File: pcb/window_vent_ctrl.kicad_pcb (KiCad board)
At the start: 2 copper layers, 70 x 50 mm, 32 parts, among them J1 12V IN, J2 FAN 0 intake, J3 FAN 1 exhaust, J4 MOTOR, J5 SCD40, J6 AS5600, J7 DS18B20 in, J8 DS18B20 out, U1 Freenove ESP32-S3 Lite, U2 TMC2209 module

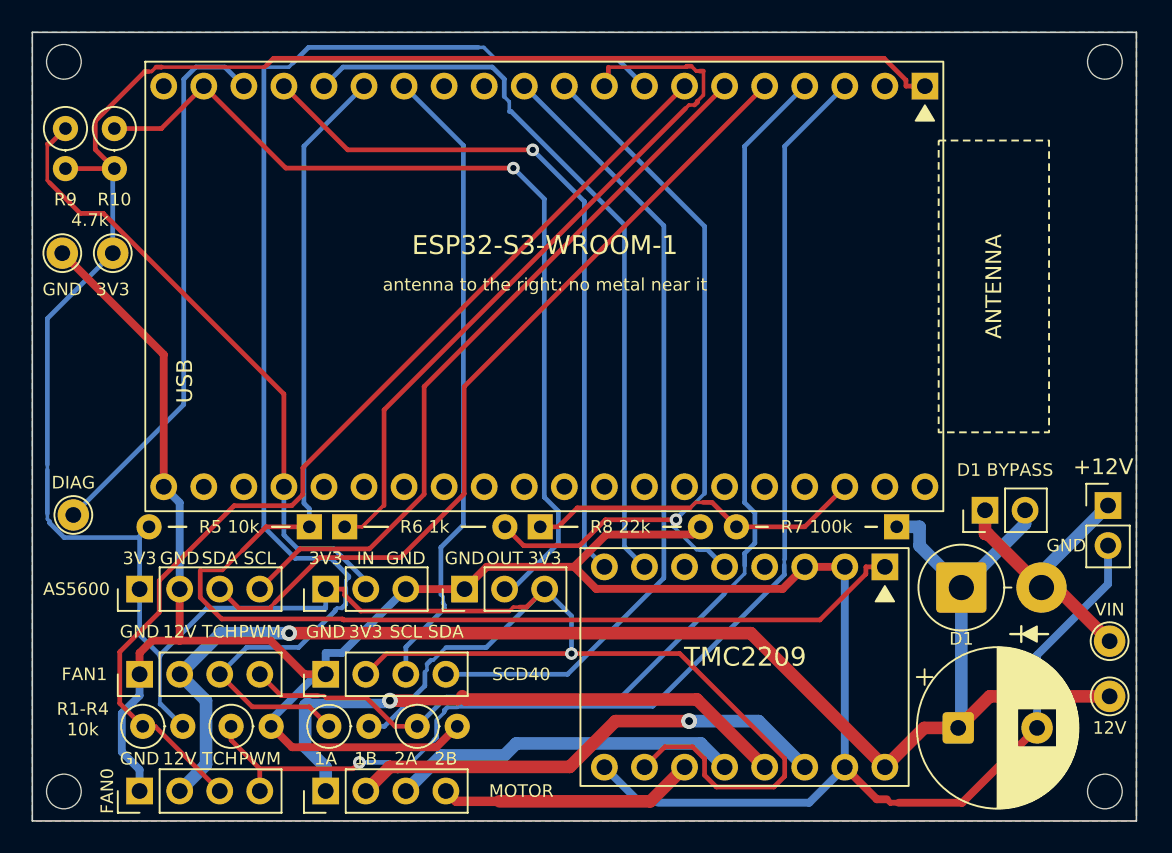
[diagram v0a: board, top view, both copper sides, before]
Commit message: PCB silkscreen: USB-UART cue, TEMP bracket, orientation sketch
Front: "USB-UART" at the board edge beside the ESP32's USB-UART connector
(replacing the footprint's "USB"); a dotted bracket from J7 and J8 to
"TEMP"; SCD40 and MOTOR at FAN1's spacing; FAN1/SCD40 pin labels at the
same 2 mm as the other rows; C1's "+", J1's GND and D1 moved clear.
Back: title and URL clear of the vias, with a small sketch of the board
between "outdoor (top edge)" and "indoor (bottom edge)". DRC clean.

Co-Authored-By: Claude Opus 5.5 <noreply@anthropic.com>
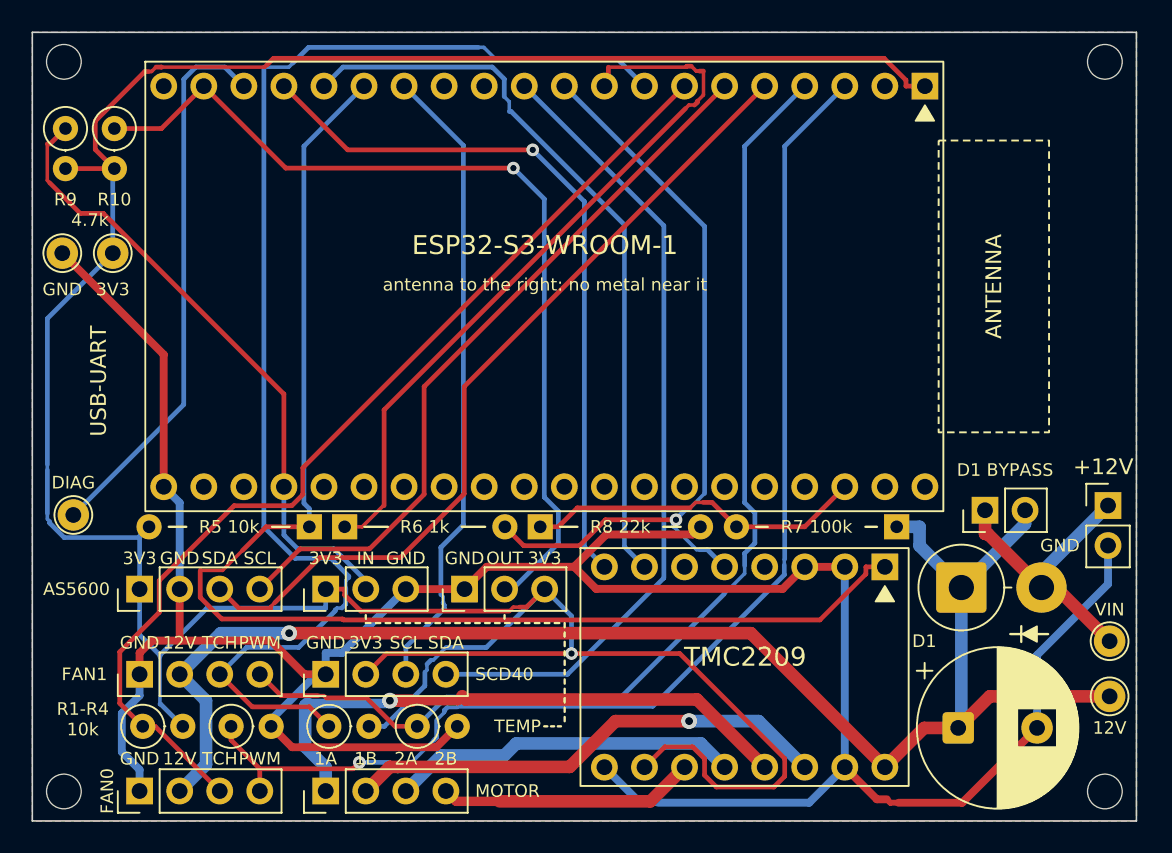
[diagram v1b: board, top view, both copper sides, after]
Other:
- board text added: "TEMP"
- board text added: "USB-UART"
- board text added: "indoor (bottom edge)"
- board text added: "outdoor (top edge)"
- board text added: "this PCB"
- board text removed: "J7: DS18B20 in (GPIO 21) J8: DS18B20 out (GPIO 14) C1: 220 uF 50 V"
- board text removed: "room side (bottom edge)"
- board text removed: "window side (top edge)"

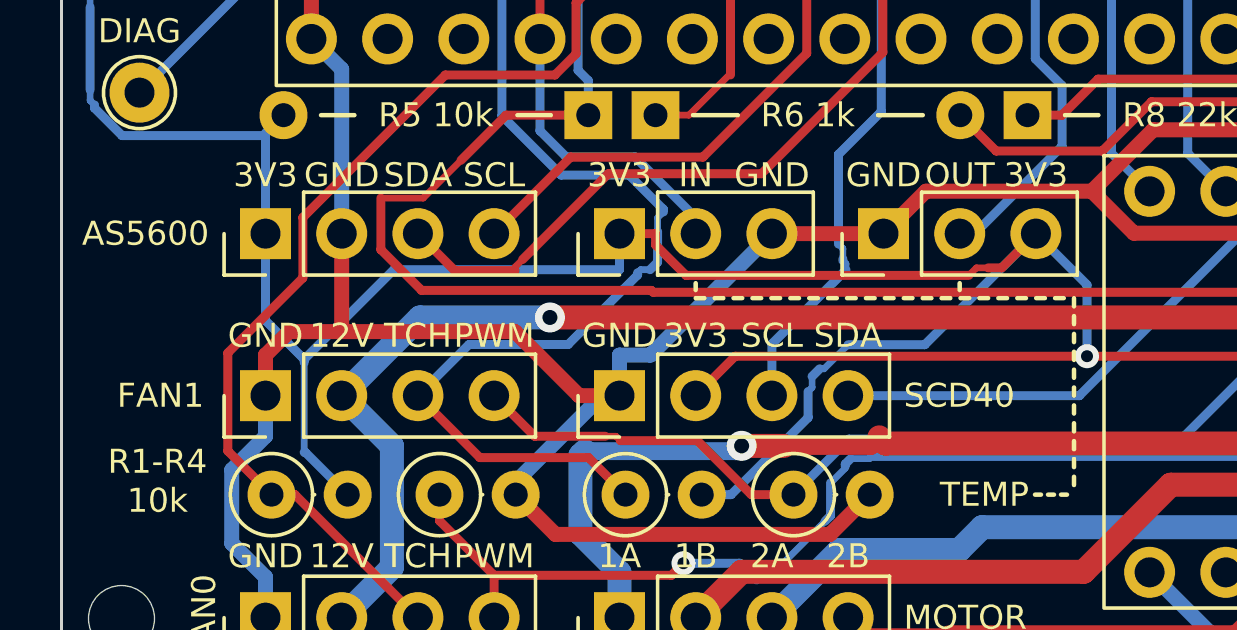
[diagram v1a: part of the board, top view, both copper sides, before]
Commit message: PCB silkscreen: FAN1 down arrow, AS5600 POS and SCD40 CO2 labels
A small down triangle above FAN1 (the exhaust, the bottom duct); a second
line under AS5600 ("POS") and SCD40 ("CO2", with a subscript 2). DRC clean.

Co-Authored-By: Claude Opus 5.5 <noreply@anthropic.com>
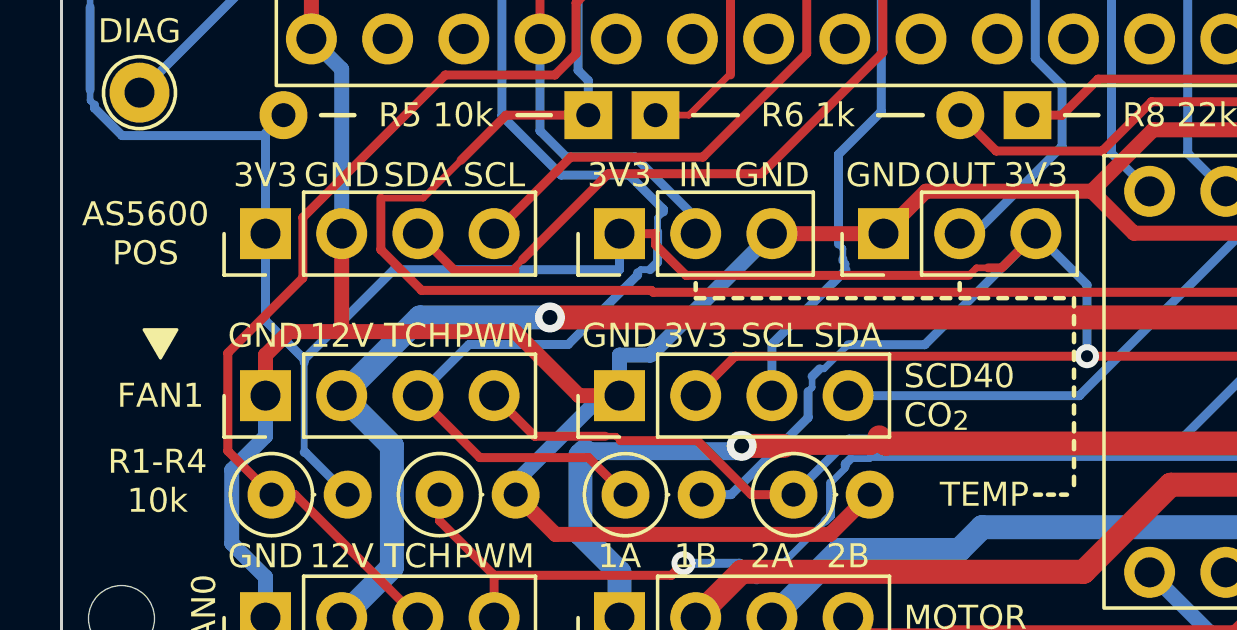
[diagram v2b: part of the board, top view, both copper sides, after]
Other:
- board text added: "CO_{2}"
- board text added: "POS"
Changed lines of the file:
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@@
+	(gr_poly
+		(pts
+			(xy 102.75 138.5) (xy 103.85 138.5) (xy 103.3 139.45)
+		)
+		(stroke
+			(width 0.1)
+			(type default)
+		)
+		(fill yes)
+		(layer "F.SilkS")
+	)
 	(gr_poly
 		(pts
@@
 		(layer "Edge.Cuts")
 	)
+	(gr_text "CO_{2}"
+		(at 128.074286 141.35 0)
+		(layer "F.SilkS")
+		(effects
+			(font
+				(size 0.8 0.8)
+				(thickness 0.15)
+			)
+			(justify left)
+		)
+	)
 	(gr_text "GND"
 		(at 101.9 116.3 0)
@@
 		)
 	)
+	(gr_text "POS"
+		(at 102.8 135.95 0)
+		(layer "F.SilkS")
+		(effects
+			(font
+				(size 0.8 0.8)
+				(thickness 0.15)
+			)
+		)
+	)
 	(gr_text "R1-R4"
 		(at 103.2 142.9 0)
@@
 	)
 	(gr_text "SCD40"
-		(at 128.074286 140.7 0)
+		(at 128.074286 140.05 0)
 		(layer "F.SilkS")
 		(effects
@@
 	)
 	(gr_text "AS5600"
-		(at 102.8 135.3 0)
-		(layer "F.SilkS")
-		(effects
+		(at 102.8 134.65 0)
+		(layer "F.SilkS")
+		(effects

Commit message: Controller PCB v1.1: solder jumper JP2 joins GPIO 21 to GPIO 3 (audio mode)
JP2, open by default, on the back under the ESP32: bridge it to read a
microphone on J7 with GPIO 3 (ADC1). The board is re-routed; the routing
now keeps vias off every silkscreen label. The v1.0 Gerber zip stays (the
boards already ordered). Docs, Pins.h and the wiring diagram mention JP2.

Co-Authored-By: Claude Opus 5.5 <noreply@anthropic.com>
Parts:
- added JP2: AUDIO, Jumper:SolderJumper-2_P1.3mm_Open_RoundedPad1.0x1.5mm, B.Cu at (117.0, 124.0)
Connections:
- U1 pad 12: unconnected-(U1-GPIO3-Pad12) -> /MIC
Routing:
- net /MIC: track 0.00 -> 29.9 mm, vias 0 -> 1
- net /+3V3: track 197.1 -> 170.2 mm, vias 1 -> 2
- net /TMC_STEP: track 46.9 -> 63.8 mm
- net /TMC_UART: track 48.9 -> 64.6 mm, vias 1 -> 0
- net /FAN0_TACH: track 64.7 -> 77.6 mm, vias 0 -> 3
- net /FAN1_PWM: track 69.1 -> 80.8 mm, vias 0 -> 2
- net /TMC_EN: track 85.1 -> 73.5 mm
- net /+12V: track 96.2 -> 103.2 mm
- net /ENC_SCL: track 46.7 -> 53.2 mm, vias 0 -> 1
- net /FAN1_TACH: track 81.5 -> 86.9 mm, vias 0 -> 1
- net /MOT_1A: track 37.2 -> 31.9 mm, vias 1 -> 0
- net /GND: track 173.6 -> 178.8 mm, vias 0 -> 1
- net /DQ_IN: track 40.3 -> 44.5 mm, vias 0 -> 1
- net /SCD_SDA: track 51.2 -> 47.5 mm, vias 0 -> 2
- net /TMC_DIAG: track 35.2 -> 31.7 mm
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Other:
- board text added: "GPIO21-GPIO3"
- board text added: "JP2 AUDIO"
- board text added: "WINDOW VENT CONTROLLER v1.1"
- board text removed: "WINDOW VENT CONTROLLER v1.0"
